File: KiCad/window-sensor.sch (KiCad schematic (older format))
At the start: 16 parts, among them J1 Conn_01x05_Male, U3 74HC86

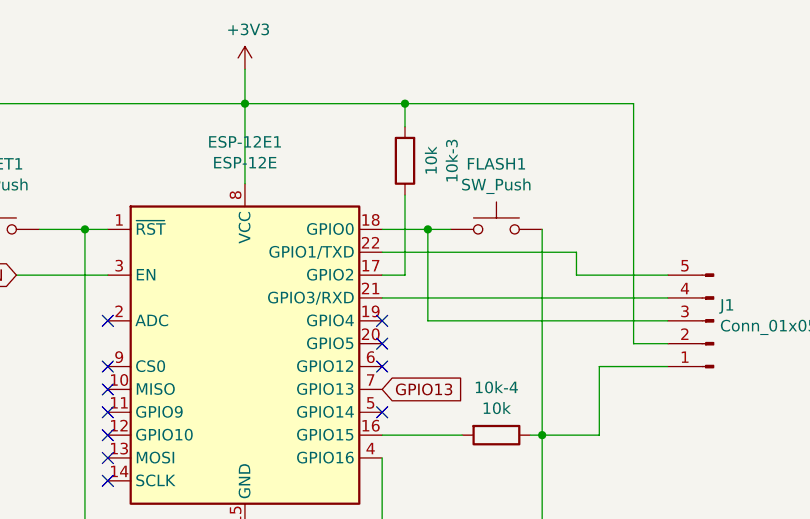
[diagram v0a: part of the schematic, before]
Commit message: Circuit corrected. Pullup now at GPIO0 instead of GPIO2.
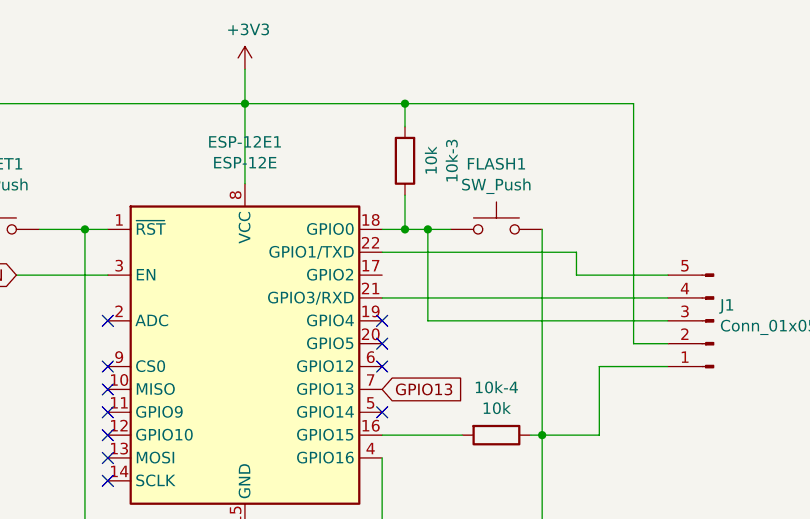
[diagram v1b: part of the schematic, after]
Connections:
- net at ESP-12E1.17 (GPIO2): no longer 10k-3.1
- net at ESP-12E1.18 (GPIO0), FLASH1.1, J1.3 (Pin_3): now also 10k-3.1
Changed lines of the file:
@@
 $EndComp
 Wire Wire Line
-	5900 2850 6100 2850
+	5900 2850 6000 2850
 Wire Wire Line
 	4400 2850 4600 2850
@@
 $EndComp
 Wire Wire Line
-	5900 3050 6000 3050
-Wire Wire Line
-	6000 3050 6000 2700
-Wire Wire Line
 	6000 2400 6000 2300
 Connection ~ 6000 2300
@@
 Wire Wire Line
 	3800 2300 5300 2300
+Wire Wire Line
+	6000 2700 6000 2850
+Connection ~ 6000 2850
+Wire Wire Line
+	6000 2850 6100 2850
 $EndSCHEMATC
